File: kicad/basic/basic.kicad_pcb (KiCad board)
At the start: 2 copper layers, 50 x 50 mm, 16 parts, among them P1 CONN_01X15, P2 CONN_01X15, P3 CONN_01X15, P4 CONN_01X15, P5 CONN_01X01, P6 CONN_01X01, P7 CONN_01X01, P8 CONN_01X01

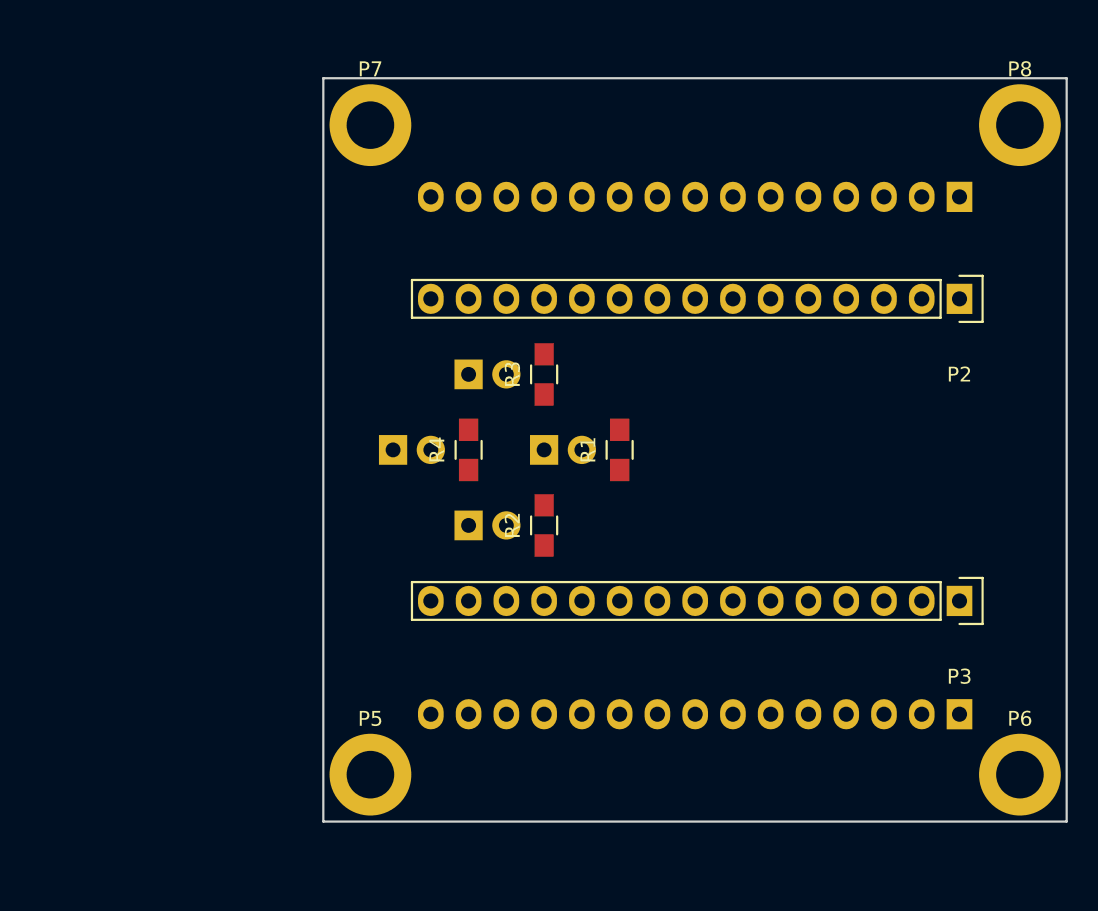
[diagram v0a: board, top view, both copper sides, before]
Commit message: Breakout only the GPIO
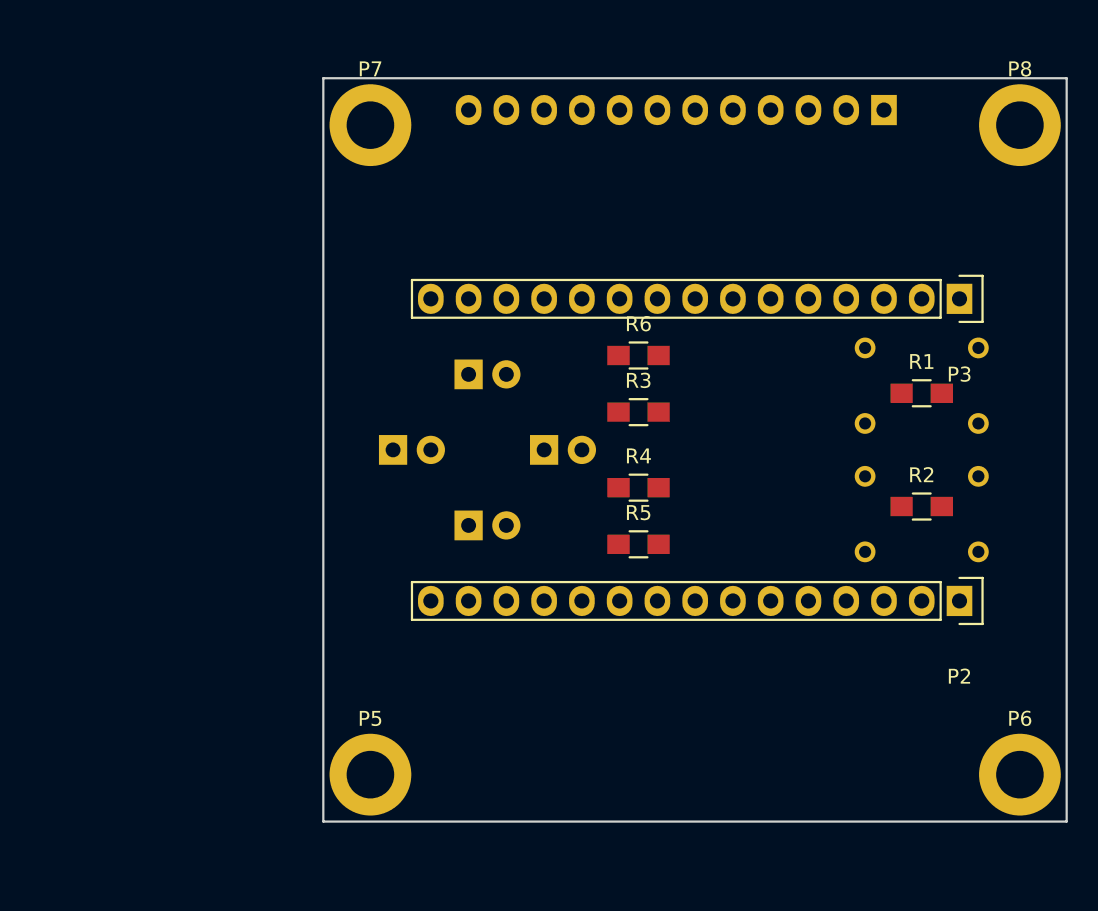
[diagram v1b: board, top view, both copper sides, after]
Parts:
- removed P4: CONN_01X15, Socket_Strips:Socket_Strip_Straight_1x15
- added R5: 220, Resistors_SMD:R_0805_HandSoldering, F.Cu at (161.2, 106.3)
- added R6: 220, Resistors_SMD:R_0805_HandSoldering, F.Cu at (161.2, 93.7)
- added SW1: SW_PUSH, Buttons_Switches_ThroughHole:SW_PUSH_SMALL, B.Cu at (180.3, 95.7)
- added SW2: SW_PUSH, Buttons_Switches_ThroughHole:SW_PUSH_SMALL, B.Cu at (180.3, 104.3)
- P1: value CONN_01X15 -> CONN_01X12; footprint Socket_Strips:Socket_Strip_Straight_1x15 -> Socket_Strips:Socket_Strip_Straight_1x12
- R1, R2: value R -> 10K
- R3, R4: value R -> 220
- moved R2 25.4 mm to (180.3, 103.8), turned to 0 degrees
- moved R1 20.7 mm to (180.3, 96.2), turned to 0 degrees
- moved P2 20.3 mm to (182.8, 110.2)
- moved P3 20.3 mm to (182.8, 89.8)
- moved R4 11.7 mm to (161.2, 102.5), turned to 0 degrees
- moved P1 7.74 mm to (177.7, 77.1)
- moved R3 6.84 mm to (161.2, 97.5), turned to 0 degrees
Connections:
- P1 pad 1: /3V3 -> GND
- P1 pad 10: Net-(P1-Pad10) -> GIPO13
- P1 pad 11: Net-(P1-Pad11) -> GIPO14
- P1 pad 12: Net-(P1-Pad12) -> GIPO15
- P1 pad 2: GND -> A0
- P1 pad 3: Net-(P1-Pad3) -> GIPO0
- P1 pad 4: Net-(P1-Pad4) -> GIPO1
- P1 pad 5: Net-(P1-Pad5) -> GIPO2
- P1 pad 6: Net-(P1-Pad6) -> GIPO3
- P1 pad 7: GND -> GIPO4
- P1 pad 8: /3V3 -> GIPO5
- P1 pad 9: Net-(P1-Pad9) -> GIPO12
- P2 pad 1: /3V3 -> A0
- P2 pad 10: Net-(P1-Pad10) -> GND
- P2 pad 11: Net-(P1-Pad11) -> 3V3
- P2 pad 12: Net-(P1-Pad12) -> Net-(P2-Pad12)
- P2 pad 13: Net-(P1-Pad13) -> Net-(P2-Pad13)
- P2 pad 14: Net-(P1-Pad14) -> GND
- P2 pad 15: Net-(P1-Pad15) -> Net-(P2-Pad15)
- P2 pad 2: GND -> Net-(P2-Pad2)
- P2 pad 3: Net-(P1-Pad3) -> Net-(P2-Pad3)
- P2 pad 4: Net-(P1-Pad4) -> Net-(P2-Pad4)
- P2 pad 5: Net-(P1-Pad5) -> Net-(P2-Pad5)
- P2 pad 6: Net-(P1-Pad6) -> Net-(P2-Pad6)
- P2 pad 7: GND -> Net-(P2-Pad7)
- P2 pad 8: /3V3 -> Net-(P2-Pad8)
- P2 pad 9: Net-(P1-Pad9) -> Net-(P2-Pad9)
- P3 pad 1: Net-(P3-Pad1) -> 3V3
- P3 pad 10: GND -> 3V3
- P3 pad 11: Net-(P3-Pad11) -> GIPO2
- P3 pad 12: Net-(P3-Pad12) -> GIPO0
- P3 pad 13: Net-(P3-Pad13) -> GIPO4
- P3 pad 14: GND -> GIPO5
- P3 pad 2: Net-(P3-Pad2) -> GND
- P3 pad 3: Net-(P3-Pad3) -> GPIO1
- P3 pad 4: Net-(P3-Pad4) -> GIPO3
- P3 pad 5: Net-(P3-Pad5) -> GIPO15
- P3 pad 6: Net-(P3-Pad6) -> GIPO13
- P3 pad 7: Net-(P3-Pad7) -> GIPO12
- P3 pad 8: Net-(P3-Pad8) -> GIPO14
- P3 pad 9: Net-(P3-Pad9) -> GND
- R1 pad 1: Net-(D1-Pad2) -> GND
- R1 pad 2: Net-(P1-Pad9) -> GIPO5
- R2 pad 1: Net-(D2-Pad2) -> GND
- R2 pad 2: Net-(P1-Pad6) -> GIPO4
- R3 pad 1: Net-(D3-Pad2) -> Net-(D1-Pad2)
- R3 pad 2: Net-(P1-Pad5) -> GIPO15
- R4 pad 2: Net-(P1-Pad10) -> GIPO12

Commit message: Through hole parts
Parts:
- removed P1: CONN_01X12, Socket_Strips:Socket_Strip_Straight_1x12
- added P4: CONN_01X06, Socket_Strips:Socket_Strip_Straight_1x06, F.Cu at (167.6, 122.9)
- added P9: CONN_01X06, Socket_Strips:Socket_Strip_Straight_1x06, F.Cu at (167.6, 77.1)
- D1, D2, D3, D4, SW1, SW2: moved to F.Cu
- P2, P3: moved to B.Cu
- R1, R2, R3, R4, R5, R6: footprint Resistors_SMD:R_0805_HandSoldering -> Resistors_ThroughHole:Resistor_Horizontal_RM10mm
- moved R3 18.9 mm to (154.9, 115.2)
- moved R4 18.9 mm to (154.9, 84.8)
- moved D1 17.0 mm to (147.2, 115.2)
- moved D4 15.5 mm to (147.2, 84.8)
- moved R2 15.3 mm to (170.1, 115.2), turned to 90 degrees
- moved SW2 12.3 mm to (178.7, 116.5)
- moved SW1 12.0 mm to (178.7, 83.7)
- moved R1 10.2 mm to (170.1, 94.9), turned to 90 degrees
- moved R5 6.48 mm to (154.9, 105.1)
- moved R6 6.48 mm to (154.9, 94.9)
- moved D2 2.54 mm to (147.2, 105.1)
- moved D3 2.54 mm to (147.2, 94.9)

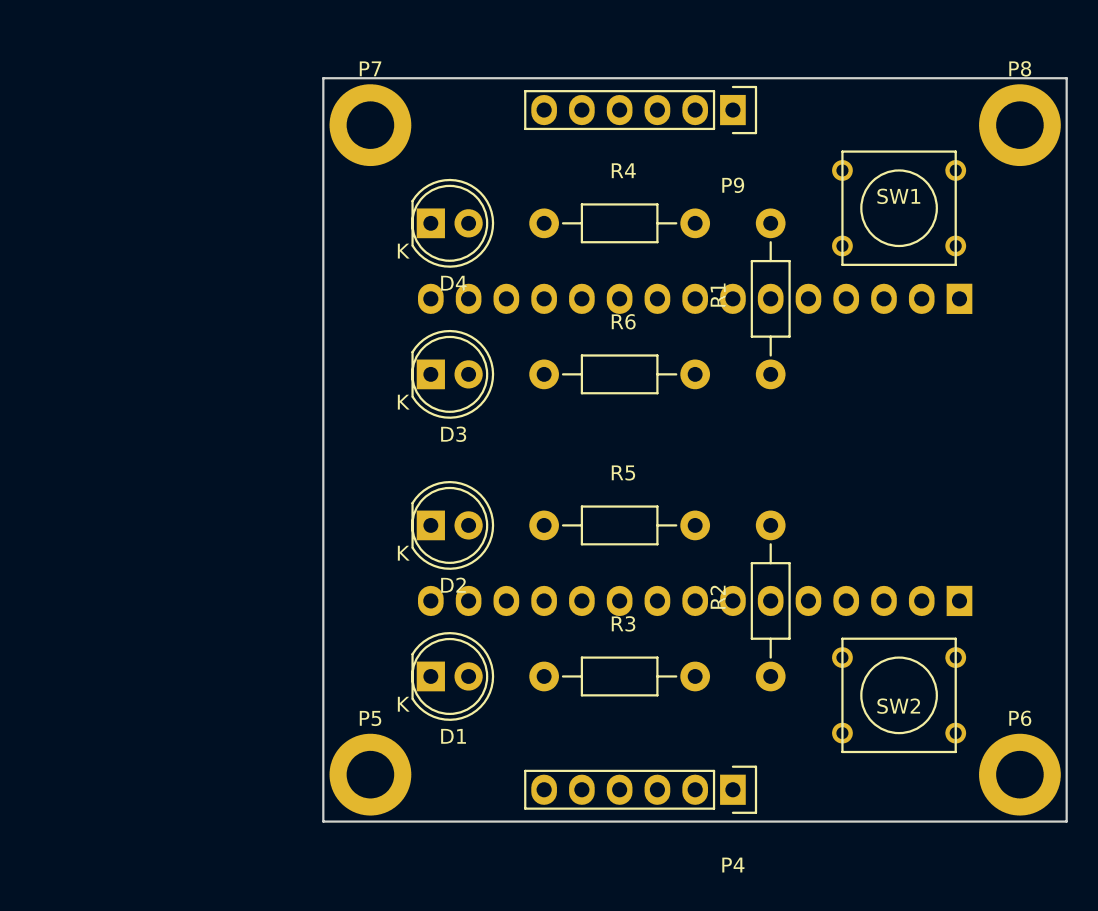
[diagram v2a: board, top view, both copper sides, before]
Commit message: Wider nodemcu footprint
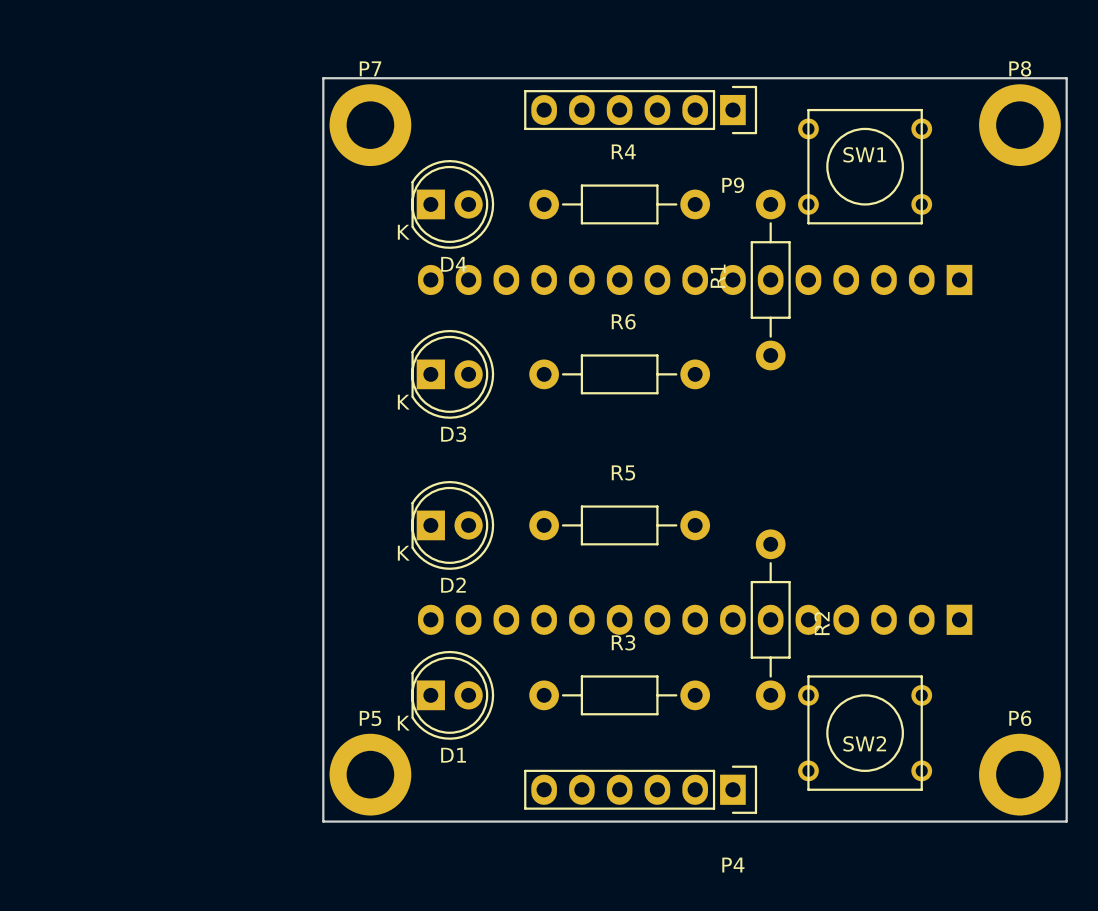
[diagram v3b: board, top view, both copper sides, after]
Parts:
- moved R2 8.89 mm to (170.1, 106.3), turned to 270 degrees
- moved SW1 3.61 mm to (176.4, 81.0)
- moved SW2 3.42 mm to (176.4, 119.0)
- moved D1 1.27 mm to (147.2, 116.5)
- moved D4 1.27 mm to (147.2, 83.5)
- moved P2 1.27 mm to (182.8, 111.4)
- moved P3 1.27 mm to (182.8, 88.6)
- moved R3 1.27 mm to (154.9, 116.5)
- moved R4 1.27 mm to (154.9, 83.5)
- moved R1 1.27 mm to (170.1, 93.7)
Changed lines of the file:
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@@
     (area 139.924999 74.924999 190.075001 125.075001)
     (thickness 1.6)
-    (drawings 14)
+    (drawings 11)
     (tracks 0)
     (zones 0)
@@
   )
   (module LEDs:LED-5MM placed (layer F.Cu)
-    (at 147.232 115.24)
+    (at 147.232 116.51)
     (descr "LED 5mm round vertical")
     (tags "LED 5mm round vertical")
@@
   )
   (module LEDs:LED-5MM placed (layer F.Cu)
-    (at 147.232 84.76)
+    (at 147.232 83.49)
     (descr "LED 5mm round vertical")
     (tags "LED 5mm round vertical")
@@
   )
   (module Buttons_Switches_ThroughHole:SW_PUSH_SMALL (layer F.Cu)
-    (at 178.728 83.744)
+    (at 176.442 80.95)
     (fp_text reference SW1 (at 0 -0.762) (layer F.SilkS)
       (effects (font (size 1 1) (thickness 0.15)))
@@
   )
   (module Buttons_Switches_ThroughHole:SW_PUSH_SMALL (layer F.Cu)
-    (at 178.728 116.51 180)
+    (at 176.442 119.05 180)
     (fp_text reference SW2 (at 0 -0.762 180) (layer F.SilkS)
       (effects (font (size 1 1) (thickness 0.15)))
@@
   )
   (module Socket_Strips:Socket_Strip_Straight_1x15 (layer B.Cu)
-    (at 182.792 110.16 180)
+    (at 182.792 111.43 180)
     (descr "Through hole socket strip")
     (tags "socket strip")
@@
   )
   (module Socket_Strips:Socket_Strip_Straight_1x15 (layer B.Cu)
-    (at 182.792 89.84 180)
+    (at 182.792 88.57 180)
     (descr "Through hole socket strip")
     (tags "socket strip")
@@
   )
   (module Resistors_ThroughHole:Resistor_Horizontal_RM10mm (layer F.Cu)
-    (at 170.092 94.92 90)
+    (at 170.092 93.65 90)
     (descr "Resistor, Axial,  RM 10mm, 1/3W")
     (tags "Resistor Axial RM 10mm 1/3W")
@@
   )
   (module Resistors_ThroughHole:Resistor_Horizontal_RM10mm (layer F.Cu)
-    (at 170.092 115.24 90)
+    (at 170.092 106.35 270)
     (descr "Resistor, Axial,  RM 10mm, 1/3W")
     (tags "Resistor Axial RM 10mm 1/3W")
-    (fp_text reference R2 (at 5.32892 -3.50012 90) (layer F.SilkS)
-      (effects (font (size 1 1) (thickness 0.15)))
-    )
-    (fp_text value 10K (at 5.08 0 90) (layer F.Fab)
+    (fp_text reference R2 (at 5.32892 -3.50012 270) (layer F.SilkS)
+      (effects (font (size 1 1) (thickness 0.15)))
+    )
+    (fp_text value 10K (at 5.08 0 270) (layer F.Fab)
       (effects (font (size 1 1) (thickness 0.15)))
     )
@@
     (fp_line (start 2.54 0) (end 1.27 0) (layer F.SilkS) (width 0.15))
     (fp_line (start 7.62 0) (end 8.89 0) (layer F.SilkS) (width 0.15))
-    (pad 1 thru_hole circle (at 0 0 90) (size 1.99898 1.99898) (drill 1.00076) (layers *.Cu *.SilkS *.Mask)
-      (net 1 GND))
-    (pad 2 thru_hole circle (at 10.16 0 90) (size 1.99898 1.99898) (drill 1.00076) (layers *.Cu *.SilkS *.Mask)
+    (pad 1 thru_hole circle (at 0 0 270) (size 1.99898 1.99898) (drill 1.00076) (layers *.Cu *.SilkS *.Mask)
+      (net 1 GND))
+    (pad 2 thru_hole circle (at 10.16 0 270) (size 1.99898 1.99898) (drill 1.00076) (layers *.Cu *.SilkS *.Mask)
       (net 12 GIPO4))
     (model Resistors_ThroughHole.3dshapes/Resistor_Horizontal_RM10mm.wrl
@@
   )
   (module Resistors_ThroughHole:Resistor_Horizontal_RM10mm (layer F.Cu)
-    (at 154.852 115.24)
+    (at 154.852 116.51)
     (descr "Resistor, Axial,  RM 10mm, 1/3W")
     (tags "Resistor Axial RM 10mm 1/3W")
@@
   )
   (module Resistors_ThroughHole:Resistor_Horizontal_RM10mm (layer F.Cu)
-    (at 154.852 84.76)
+    (at 154.852 83.49)
     (descr "Resistor, Axial,  RM 10mm, 1/3W")
     (tags "Resistor Axial RM 10mm 1/3W")
@@
   (gr_line (start 188.976 87.376) (end 188.976 112.776) (angle 90) (layer Dwgs.User) (width 0.2))
   (gr_line (start 140.716 87.376) (end 188.976 87.376) (angle 90) (layer Dwgs.User) (width 0.2))
-  (gr_line (start 134.52 107.62) (end 139.6 107.62) (angle 90) (layer Dwgs.User) (width 0.2))
-  (gr_line (start 134.52 92.38) (end 134.52 107.62) (angle 90) (layer Dwgs.User) (width 0.2))
-  (gr_line (start 139.6 92.38) (end 134.52 92.38) (angle 90) (layer Dwgs.User) (width 0.2))
   (dimension 25.4 (width 0.3) (layer Cmts.User)
     (gr_text "25.400 mm" (at 201.91 100 270) (layer Cmts.User)

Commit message: Labeling
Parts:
- moved P6 63.5 mm to (123.5, 118.7), turned to 270 degrees
- moved SW2 51.3 mm to (126.3, 108.3), turned to 90 degrees
- moved P4 50.8 mm to (122.5, 99.4), turned to 90 degrees
- moved P5 50.8 mm to (123.5, 75.0), turned to 270 degrees
- moved P2 49.0 mm to (133.9, 114.6), turned to 90 degrees
- moved P8 45.0 mm to (167.2, 118.7), turned to 270 degrees
- moved D1 41.7 mm to (128.8, 79.0), turned to 270 degrees
- moved R3 39.6 mm to (128.8, 86.7), turned to 270 degrees
- moved P3 36.8 mm to (156.8, 114.6), turned to 90 degrees
- moved R2 31.4 mm to (139.0, 101.9), turned to 180 degrees
- moved SW1 29.9 mm to (164.4, 108.3), turned to 270 degrees
- moved D2 27.0 mm to (140.2, 79.0), turned to 270 degrees
- moved P7 24.2 mm to (167.2, 75.0), turned to 270 degrees
- moved R5 23.5 mm to (140.2, 86.7), turned to 270 degrees
- moved P9 22.2 mm to (168.2, 99.4), turned to 90 degrees
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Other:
- board text added: "1"
- board text added: "12"
- board text added: "13"
- board text added: "14"
- board text added: "15"
- board text added: "2"
- board text added: "3"
- board text added: "4"
- board text added: "5"
- board text added: "A"
- board text added: "Denbit v1.0"
- board text added: "GND"
- board text added: "https://github.com/theapi/denbit"
